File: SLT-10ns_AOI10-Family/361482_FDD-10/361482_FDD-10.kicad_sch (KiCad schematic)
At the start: 9 parts, among them U1 12-Pin_SLx_Can

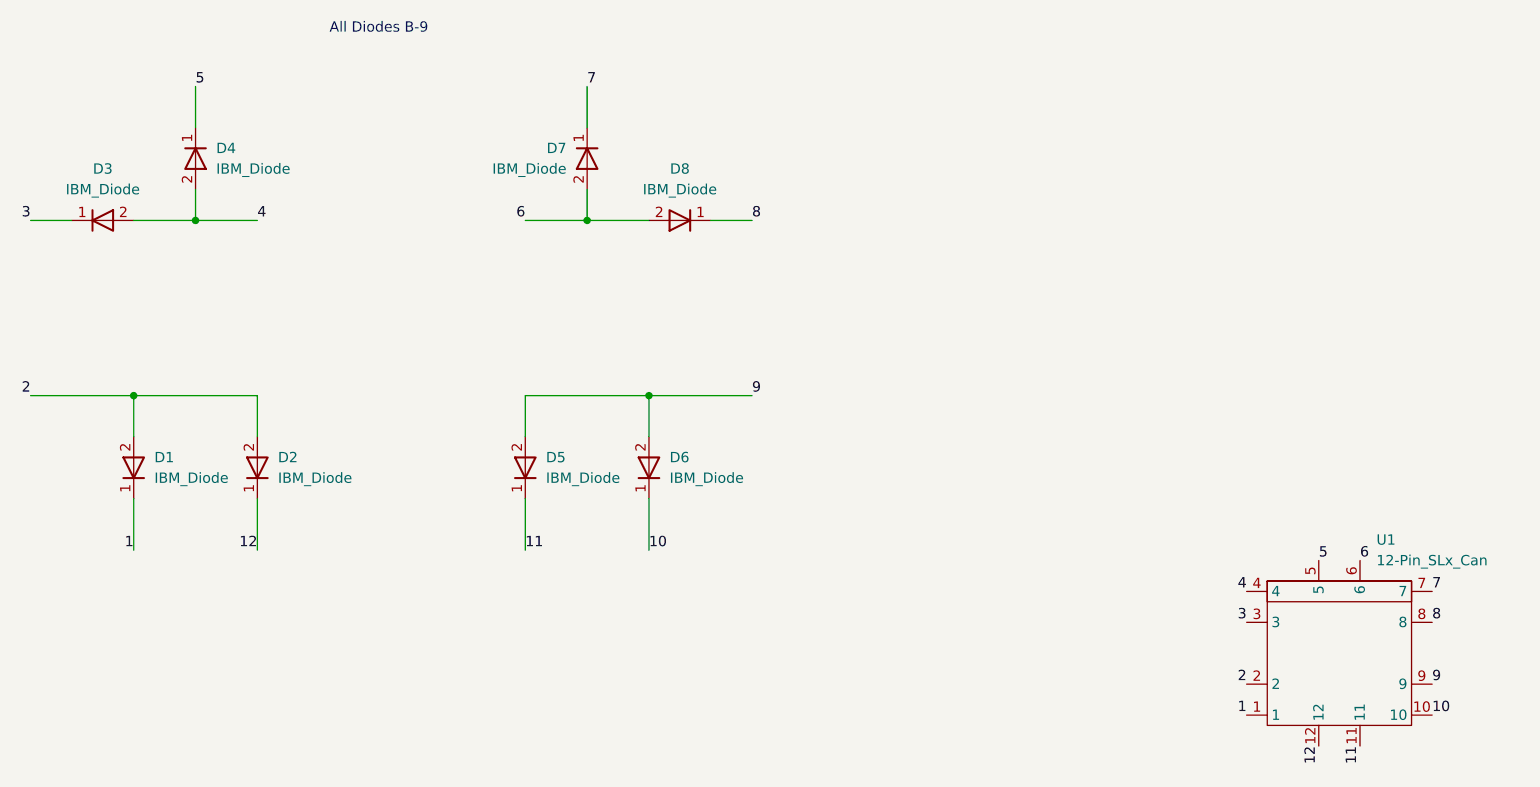
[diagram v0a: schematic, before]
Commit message: Finished off the SLT-30 family of parts, started on the SLT-700 family. Changed labeling of transistors and diodes in all schematics, but have yet to update all the pdf files. This is a TODO...
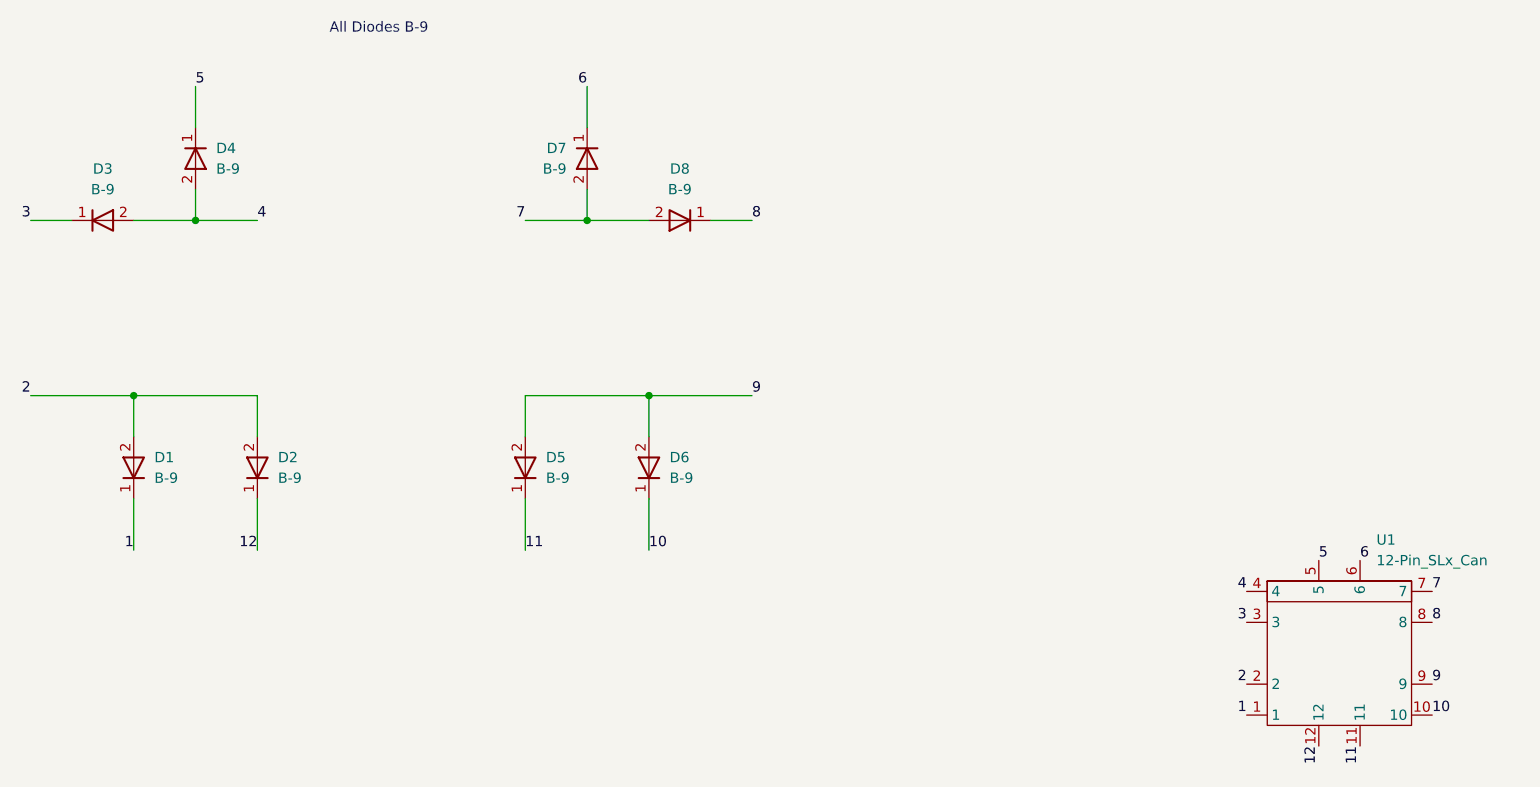
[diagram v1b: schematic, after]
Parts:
- D1, D2, D3, D4, D5, D6, D7, D8: value IBM_Diode -> B-9
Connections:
- net 6: now also D7.1 (K); no longer D7.2 (A), D8.2 (A)
- net 7: now also D7.2 (A), D8.2 (A); no longer D7.1 (K)
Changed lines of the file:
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@@
     (effects (font (size 1.27 1.27)) (justify left bottom))
   )
-  (label "6" (at 137.16 80.01 180)
+  (label "6" (at 144.78 63.5 180)
     (effects (font (size 1.27 1.27)) (justify right bottom))
   )
@@
     (effects (font (size 1.27 1.27)) (justify right bottom))
   )
-  (label "7" (at 144.78 63.5 0)
-    (effects (font (size 1.27 1.27)) (justify left bottom))
+  (label "7" (at 137.16 80.01 180)
+    (effects (font (size 1.27 1.27)) (justify right bottom))
   )
   (label "3" (at 76.2 80.01 180)
@@
       (effects (font (size 1.27 1.27)) (justify left))
     )
-    (property "Value" "IBM_Diode" (id 1) (at 99.06 73.6599 90)
+    (property "Value" "B-9" (id 1) (at 99.06 73.6599 90)
       (effects (font (size 1.27 1.27)) (justify left))
     )
@@
       (effects (font (size 1.27 1.27)) (justify right))
     )
-    (property "Value" "IBM_Diode" (id 1) (at 106.68 111.7599 90)
+    (property "Value" "B-9" (id 1) (at 106.68 111.7599 90)
       (effects (font (size 1.27 1.27)) (justify right))
     )
@@
       (effects (font (size 1.27 1.27)) (justify left))
     )
-    (property "Value" "IBM_Diode" (id 1) (at 142.24 73.6599 90)
+    (property "Value" "B-9" (id 1) (at 142.24 73.6599 90)
       (effects (font (size 1.27 1.27)) (justify left))
     )
@@
       (effects (font (size 1.27 1.27)) (justify right))
     )
-    (property "Value" "IBM_Diode" (id 1) (at 91.44 111.7599 90)
+    (property "Value" "B-9" (id 1) (at 91.44 111.7599 90)
       (effects (font (size 1.27 1.27)) (justify right))
     )
@@
     (in_bom yes) (on_board yes) (fields_autoplaced)
     (property "Reference" "D8" (id 0) (at 156.21 73.66 0))
-    (property "Value" "IBM_Diode" (id 1) (at 156.21 76.2 0))
+    (property "Value" "B-9" (id 1) (at 156.21 76.2 0))
     (property "Footprint" "Diode_SMD:D_0201_0603Metric" (id 2) (at 156.21 82.55 0)
       (effects (font (size 1.27 1.27)) hide)
@@
     (in_bom yes) (on_board yes) (fields_autoplaced)
     (property "Reference" "D3" (id 0) (at 85.09 73.66 0))
-    (property "Value" "IBM_Diode" (id 1) (at 85.09 76.2 0))
+    (property "Value" "B-9" (id 1) (at 85.09 76.2 0))
     (property "Footprint" "Diode_SMD:D_0201_0603Metric" (id 2) (at 85.09 77.47 0)
       (effects (font (size 1.27 1.27)) hide)
@@
       (effects (font (size 1.27 1.27)) (justify right))
     )
-    (property "Value" "IBM_Diode" (id 1) (at 139.7 111.7599 90)
+    (property "Value" "B-9" (id 1) (at 139.7 111.7599 90)
       (effects (font (size 1.27 1.27)) (justify right))
     )
@@
       (effects (font (size 1.27 1.27)) (justify right))
     )
-    (property "Value" "IBM_Diode" (id 1) (at 154.94 111.7599 90)
+    (property "Value" "B-9" (id 1) (at 154.94 111.7599 90)
       (effects (font (size 1.27 1.27)) (justify right))
     )
@@
   (symbol_instances
     (path "/801d24ff-be6b-468d-a51b-7691568aa1d6"
-      (reference "D1") (unit 1) (value "IBM_Diode") (footprint "Diode_SMD:D_0201_0603Metric")
+      (reference "D1") (unit 1) (value "B-9") (footprint "Diode_SMD:D_0201_0603Metric")
     )
     (path "/15a433c4-0335-46e4-884c-814357806383"
-      (reference "D2") (unit 1) (value "IBM_Diode") (footprint "Diode_SMD:D_0201_0603Metric")
+      (reference "D2") (unit 1) (value "B-9") (footprint "Diode_SMD:D_0201_0603Metric")
     )
     (path "/b60d9340-c16c-48dd-8b20-3b5943f6c8ab"
-      (reference "D3") (unit 1) (value "IBM_Diode") (footprint "Diode_SMD:D_0201_0603Metric")
+      (reference "D3") (unit 1) (value "B-9") (footprint "Diode_SMD:D_0201_0603Metric")
     )
     (path "/096216c5-6902-43a5-8004-8a4114c8baa4"
-      (reference "D4") (unit 1) (value "IBM_Diode") (footprint "Diode_SMD:D_0201_0603Metric")
+      (reference "D4") (unit 1) (value "B-9") (footprint "Diode_SMD:D_0201_0603Metric")
     )
     (path "/e1f12525-18b0-44bc-a18d-820be7b9946e"
-      (reference "D5") (unit 1) (value "IBM_Diode") (footprint "Diode_SMD:D_0201_0603Metric")
+      (reference "D5") (unit 1) (value "B-9") (footprint "Diode_SMD:D_0201_0603Metric")
     )
     (path "/e5207290-41d1-4708-be96-2b2603b0ffee"
-      (reference "D6") (unit 1) (value "IBM_Diode") (footprint "Diode_SMD:D_0201_0603Metric")
+      (reference "D6") (unit 1) (value "B-9") (footprint "Diode_SMD:D_0201_0603Metric")
     )
     (path "/1be5506a-07a3-447d-b379-4e04e402bbb9"
-      (reference "D7") (unit 1) (value "IBM_Diode") (footprint "Diode_SMD:D_0201_0603Metric")
+      (reference "D7") (unit 1) (value "B-9") (footprint "Diode_SMD:D_0201_0603Metric")
     )
     (path "/8e4b9e6c-d9b9-437f-9616-3123e2a2c38e"
-      (reference "D8") (unit 1) (value "IBM_Diode") (footprint "Diode_SMD:D_0201_0603Metric")
+      (reference "D8") (unit 1) (value "B-9") (footprint "Diode_SMD:D_0201_0603Metric")
     )
     (path "/75e072b9-86c1-407b-a1c4-16b7a7044004"
